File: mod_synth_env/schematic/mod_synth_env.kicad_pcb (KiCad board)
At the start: 2 copper layers, 40.6 x 109.2 mm, 30 parts, among them J1 AudioJack2, J2 AudioJack2, J3 Conn_02x08_Odd_Even, J4 Conn_01x07_Female, J5 Conn_01x07_Male, SW1 SW_Push, SW2 SW_SPDT, U1 TL072

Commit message: Add missing +12v to U1
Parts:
- removed REF** (x2): MountingHole_3.2mm_M3_Pad, MountingHole:MountingHole_3.2mm_M3_Pad
- R5: value R100k -> 100k or 10k
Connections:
- U1 pad 8: Net-(U1-Pad8) -> +12V
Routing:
- net +12V: track 77.7 -> 81.4 mm
- net GND: vias 1 -> 2

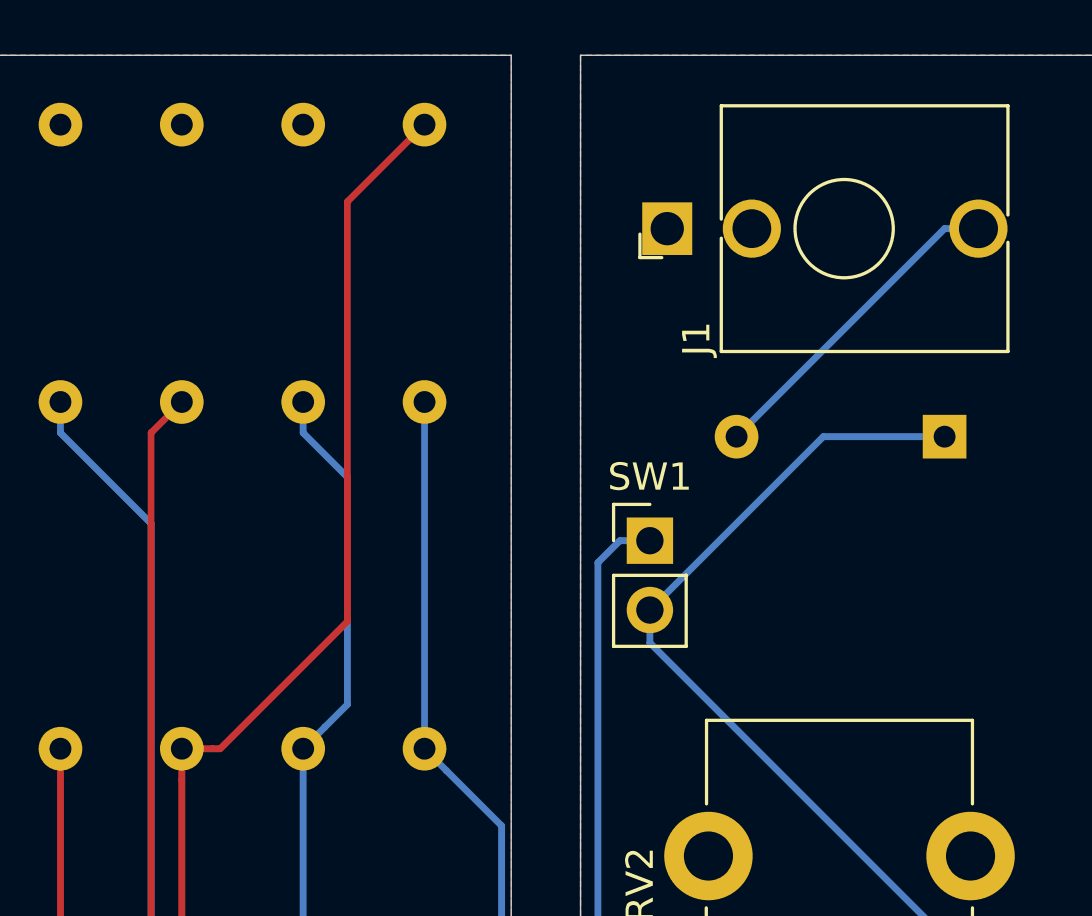
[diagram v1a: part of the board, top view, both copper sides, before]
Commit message: Re-add missing mounting hole
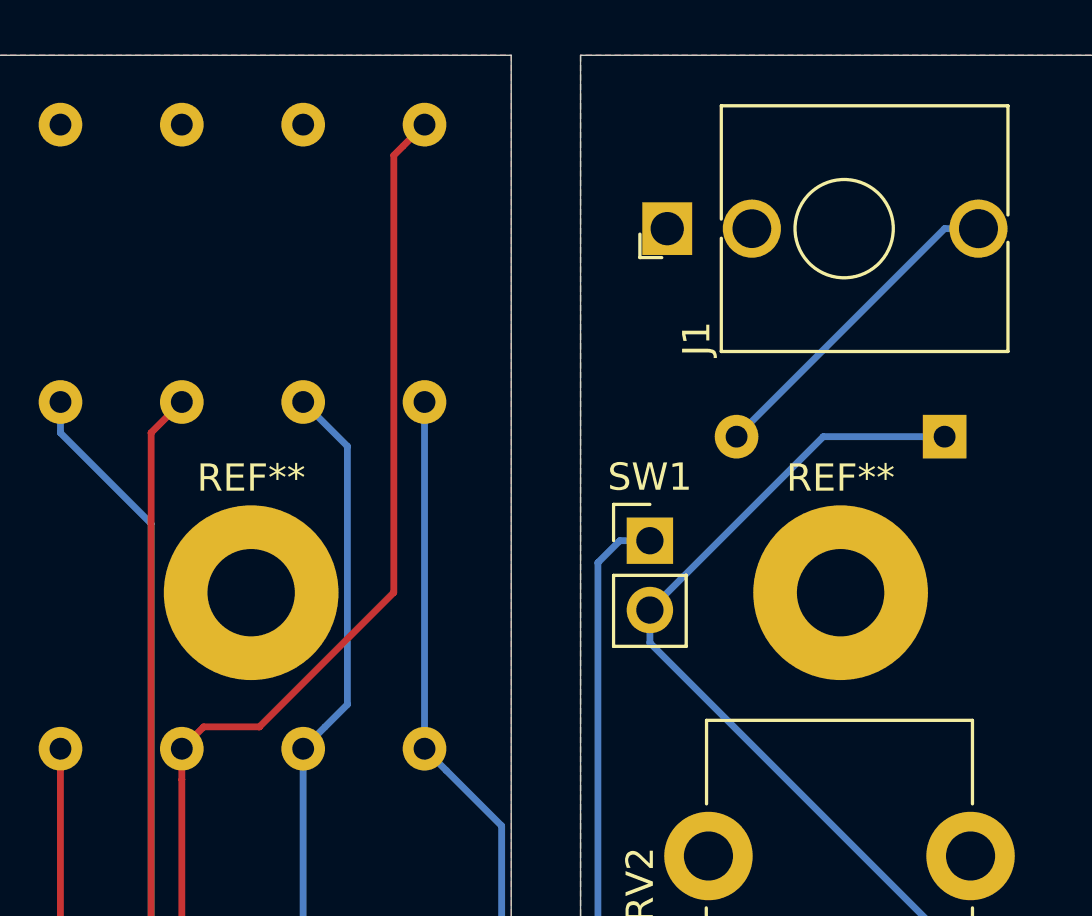
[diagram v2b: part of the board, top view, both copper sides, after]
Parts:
- added REF**: MountingHole_3.2mm_M3_Pad, MountingHole:MountingHole_3.2mm_M3_Pad, F.Cu at (47.6, 45.1)
- added REF**: MountingHole_3.2mm_M3_Pad, MountingHole:MountingHole_3.2mm_M3_Pad, F.Cu at (69.2, 45.1)
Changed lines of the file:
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@@
     (tracks 163)
     (zones 0)
-    (modules 28)
+    (modules 30)
     (nets 34)
   )
@@
     (add_net "Net-(J3-Pad16)")
     (add_net "Net-(R2-Pad1)")
+  )
+  (module MountingHole:MountingHole_3.2mm_M3_Pad (layer F.Cu)
+    (at 47.625 45.085)
+    (descr "Mounting Hole 3.2mm, M3")
+    (tags "mounting hole 3.2mm m3")
+    (attr virtual)
+    (fp_text reference REF** (at 0 -4.2) (layer F.SilkS)
+      (effects (font (size 1 1) (thickness 0.15)))
+    )
+    (fp_text value MountingHole_3.2mm_M3_Pad (at 0 4.2) (layer F.Fab)
+      (effects (font (size 1 1) (thickness 0.15)))
+    )
+    (fp_circle (center 0 0) (end 3.45 0) (layer F.CrtYd) (width 0.05))
+    (fp_circle (center 0 0) (end 3.2 0) (layer Cmts.User) (width 0.15))
+    (fp_text user %R (at 0.3 0) (layer F.Fab)
+      (effects (font (size 1 1) (thickness 0.15)))
+    )
+    (pad 1 thru_hole circle (at 0 0) (size 6.4 6.4) (drill 3.2) (layers *.Cu *.Mask))
+  )
+  (module MountingHole:MountingHole_3.2mm_M3_Pad (layer F.Cu)
+    (at 69.215 45.085)
+    (descr "Mounting Hole 3.2mm, M3")
+    (tags "mounting hole 3.2mm m3")
+    (attr virtual)
+    (fp_text reference REF** (at 0 -4.2) (layer F.SilkS)
+      (effects (font (size 1 1) (thickness 0.15)))
+    )
+    (fp_text value MountingHole_3.2mm_M3_Pad (at 0 4.2) (layer F.Fab)
+      (effects (font (size 1 1) (thickness 0.15)))
+    )
+    (fp_circle (center 0 0) (end 3.45 0) (layer F.CrtYd) (width 0.05))
+    (fp_circle (center 0 0) (end 3.2 0) (layer Cmts.User) (width 0.15))
+    (fp_text user %R (at 0.3 0) (layer F.Fab)
+      (effects (font (size 1 1) (thickness 0.15)))
+    )
+    (pad 1 thru_hole circle (at 0 0) (size 6.4 6.4) (drill 3.2) (layers *.Cu *.Mask))
   )
   (module mod_synth:SPDT_Switch_Vertical (layer F.Cu)
@@
   (segment (start 51.435 121.92) (end 51.435 98.425) (width 0.25) (layer B.Cu) (net 20))
   (segment (start 48.895 124.46) (end 51.435 121.92) (width 0.25) (layer B.Cu) (net 20))
-  (segment (start 50.329999 50.000001) (end 49.53 50.8) (width 0.25) (layer B.Cu) (net 21))
-  (segment (start 51.150001 49.179999) (end 50.329999 50.000001) (width 0.25) (layer B.Cu) (net 21))
-  (segment (start 51.150001 40.851371) (end 51.150001 49.179999) (width 0.25) (layer B.Cu) (net 21))
-  (segment (start 49.53 39.23137) (end 51.150001 40.851371) (width 0.25) (layer B.Cu) (net 21))
-  (segment (start 49.53 38.1) (end 49.53 39.23137) (width 0.25) (layer B.Cu) (net 21))
   (segment (start 51.035 93.345) (end 51.435 93.345) (width 0.25) (layer B.Cu) (net 21))
   (segment (start 48.404999 90.714999) (end 51.035 93.345) (width 0.25) (layer B.Cu) (net 21))
@@
   (segment (start 49.53 59.294998) (end 48.404999 60.419999) (width 0.25) (layer B.Cu) (net 21))
   (segment (start 49.53 50.8) (end 49.53 59.294998) (width 0.25) (layer B.Cu) (net 21))
+  (segment (start 50.329999 50.000001) (end 49.53 50.8) (width 0.25) (layer B.Cu) (net 21))
+  (segment (start 51.150001 49.179999) (end 50.329999 50.000001) (width 0.25) (layer B.Cu) (net 21))
+  (segment (start 51.150001 39.720001) (end 51.150001 49.179999) (width 0.25) (layer B.Cu) (net 21))
+  (segment (start 49.53 38.1) (end 51.150001 39.720001) (width 0.25) (layer B.Cu) (net 21))
   (segment (start 41.275 98.425) (end 40.005 97.155) (width 0.25) (layer B.Cu) (net 22))
   (segment (start 43.815 98.425) (end 41.275 98.425) (width 0.25) (layer B.Cu) (net 22))
@@
   (segment (start 50.165 103.900002) (end 56.370001 97.695001) (width 0.25) (layer F.Cu) (net 28))
   (segment (start 50.165 132.08) (end 50.165 103.900002) (width 0.25) (layer F.Cu) (net 28))
-  (segment (start 46.21637 50.8) (end 45.085 50.8) (width 0.25) (layer F.Cu) (net 28))
-  (segment (start 46.492002 50.8) (end 46.21637 50.8) (width 0.25) (layer F.Cu) (net 28))
-  (segment (start 51.150001 46.142001) (end 46.492002 50.8) (width 0.25) (layer F.Cu) (net 28))
-  (segment (start 51.150001 30.764999) (end 51.150001 46.142001) (width 0.25) (layer F.Cu) (net 28))
-  (segment (start 53.975 27.94) (end 51.150001 30.764999) (width 0.25) (layer F.Cu) (net 28))
+  (segment (start 53.175001 28.739999) (end 53.975 27.94) (width 0.25) (layer F.Cu) (net 28))
+  (segment (start 52.849999 29.065001) (end 53.175001 28.739999) (width 0.25) (layer F.Cu) (net 28))
+  (segment (start 52.849999 45.077003) (end 52.849999 29.065001) (width 0.25) (layer F.Cu) (net 28))
+  (segment (start 47.927001 50.000001) (end 52.849999 45.077003) (width 0.25) (layer F.Cu) (net 28))
+  (segment (start 45.884999 50.000001) (end 47.927001 50.000001) (width 0.25) (layer F.Cu) (net 28))
+  (segment (start 45.085 50.8) (end 45.884999 50.000001) (width 0.25) (layer F.Cu) (net 28))
   (segment (start 64.515 99.91132) (end 64.515 97.79) (width 0.25) (layer F.Cu) (net 29))
   (segment (start 63.644999 100.781321) (end 64.515 99.91132) (width 0.25) (layer F.Cu) (net 29))
